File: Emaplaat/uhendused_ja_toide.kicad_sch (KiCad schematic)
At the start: 25 parts, among them IC4 FT232RNL-TUBE, IC5 TPS54429PWPR, J5 USB4216-03-A, J6 USB-A-S-VT, J7 USB-A-S-VT, J8 Barrel_Jack

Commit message: cleanoupp T__W
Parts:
- removed J7: USB-A-S-VT, USBASVT, symbol USB-A-S-VT:USB-A-S-VT
- added J1: USB-A-S-VT, USBASVT, symbol USB-A-S-VT:USB-A-S-VT
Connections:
- net 3V3: now also J1.1
- net AGND: now also J1.4, J1.MH, J1.MH1
- net RX_pult_2: now also J1.2
- net TX_pult_2: now also J1.3
- net at IC4.19 (RESET#): now also IC4.24 (NC_2), IC4.27 (OSCI), IC4.8 (NC_1)
- net TEST: now reaches IC4.26 (TEST)
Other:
- moved on the sheet: C21, C22, C23, C24, C25, C26, C27, C28, C29, C30, C31, C32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

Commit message: qqwertrewasdfgfdsdfgfdsdfgfdsasdfghgfdsdfghgfdsasdfghgfdsasdfgfew3
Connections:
- net TEST is gone; now on net AGND: IC4.26 (TEST)
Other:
- moved on the sheet: IC4

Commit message: enamvahem valmis
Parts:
- added C1: 100u, symbol Device:C
- added C2: 47u, symbol Device:C
- added D2, D3, D4, D5, D6, D7, D8: PESD1ETH10L-QYL, PESD1ETH10LQYL, symbol PESD1ETH10L-QYL:PESD1ETH10L-QYL
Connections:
- net 12V: now also C1.1, C2.1, D8.1 (K1)
- net 3V3: now also D2.1 (K1), D4.1 (K1)
- net AGND: now also D2.2 (K2), D3.2 (K2), D4.2 (K2), D5.2 (K2), D6.2 (K2), D7.2 (K2)
- net PGND: now also C1.2, C2.2, D8.2 (K2)
- net RX_pult_1: now also D3.1 (K1)
- net RX_pult_2: now also D5.1 (K1)
- net TX_pult_1: now also D6.1 (K1)
- net TX_pult_2: now also D7.1 (K1)
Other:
- note added: "Läpaka barrel connector"
- note added: "puldilt info lugemiseks usb A ühendused, koos ESD kaitsega"
- note removed: "puldilt info lugemiseks usb A ühendused"
- moved on the sheet: C21, C22, C23, C24, C25, C26, C27, C28, C29, C30, C31, C32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

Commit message: git stuff
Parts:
- removed D5, D6, D7, D8: PESD1ETH10L-QYL, PESD1ETH10LQYL, symbol PESD1ETH10L-QYL:PESD1ETH10L-QYL
- removed J1, J6: USB-A-S-VT, USBASVT, symbol USB-A-S-VT:USB-A-S-VT
- added C270: 0.1u, symbol Device:C
- added D15, D16: LED, LED_SMD:LED_0603_1608Metric, symbol Device:LED
- added D9: PESD1ETH10L-QYL, PESD1ETH10LQYL, symbol PESD1ETH10L-QYL:PESD1ETH10L-QYL
- added R208, R209: 5.1K, symbol Device:R
- added R210, R211: 50, Resistor_SMD:R_0603_1608Metric, symbol Device:R
- renumbered C27 to C20, C28 to C21, C29 to C22, C30 to C23, C31 to C24, C1 to C25, C2 to C26, C32 to C27, C33 to C28, C34 to C29, C35 to C30, C21 to C43, C22 to C44, C23 to C45, C24 to C46, C25 to C47, C26 to C48, IC4 to IC16, IC5 to IC9, J8 to J1, J5 to J2, L2 to L1, R6 to R23, R7 to R24, R8 to R25
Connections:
- net PGND is gone; now on net AGND: C20.2, C21.2, C22.2, C23.2, C24.2, C25.2, C26.2, C30.2, IC9.15 (PAD), IC9.8 (PGND1), IC9.9 (PGND2), J1.2
- net RX_pult_1 is gone; now on an unnamed net: D3.1 (K1)
- net 12V: now also D2.1 (K1)
- net 3V3: now also IC16.4 (VCCIO), C270.1, D15.2 (A), D16.2 (A); no longer D2.1 (K1), D4.1 (K1)
- net AGND: now also C270.2, D9.2 (K2), R208.2, R209.2; no longer IC16.26 (TEST), IC16.28 (OSCO), J2.A5 (CC1), J2.A8 (SBU1), J2.B5 (CC2), J2.B8 (SBU2)
- net at C43.1, C44.1, C45.1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: now also D9.1 (K1); no longer IC16.4 (VCCIO)
- net at C47.1, IC16.15 (USBDP), J2.A6 (DP1)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: now also D4.1 (K1)
- net at IC16.24 (NC_2), IC16.8 (NC_1): no longer IC16.19 (RESET#), IC16.27 (OSCI)
- new net: J2.B5 (CC2), R209.1
- new net: J2.A5 (CC1), R208.1
- new net: IC16.23 (CBUS0), R210.1
- new net: D15.1 (K), R210.2
- new net: IC16.22 (CBUS1), R211.1
- new net: J2.A8 (SBU1), J2.B8 (SBU2)
- new net: D16.1 (K), R211.2
- now unconnected: IC16.10 (DCD#), IC16.11 (CTS#), IC16.12 (CBUS4), IC16.13 (CBUS2), IC16.14 (CBUS3), IC16.2 (DTR#), IC16.3 (RTS#), IC16.6 (RI#), IC16.9 (DSR#)
- no-connect marks 0 -> 13
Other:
- note removed: "puldilt info lugemiseks usb A ühendused, koos ESD kaitsega"
- moved on the sheet: C20, C21, C22, C23, C24, C25, C26, C27, C28, C29, C30, C43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

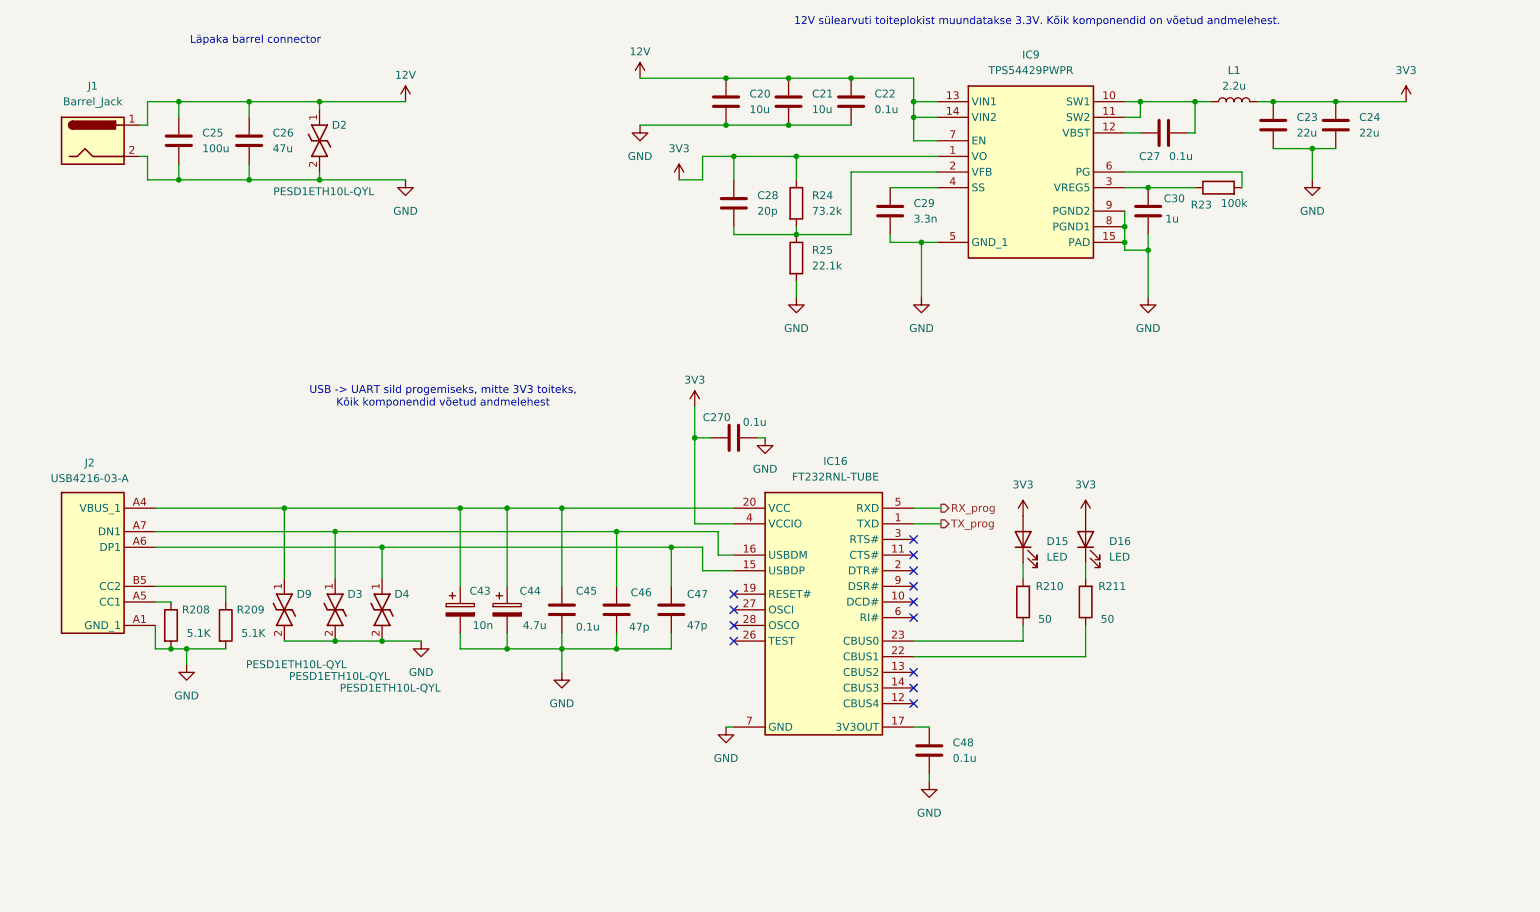
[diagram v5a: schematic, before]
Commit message: 3V3 voolud kontrollitud
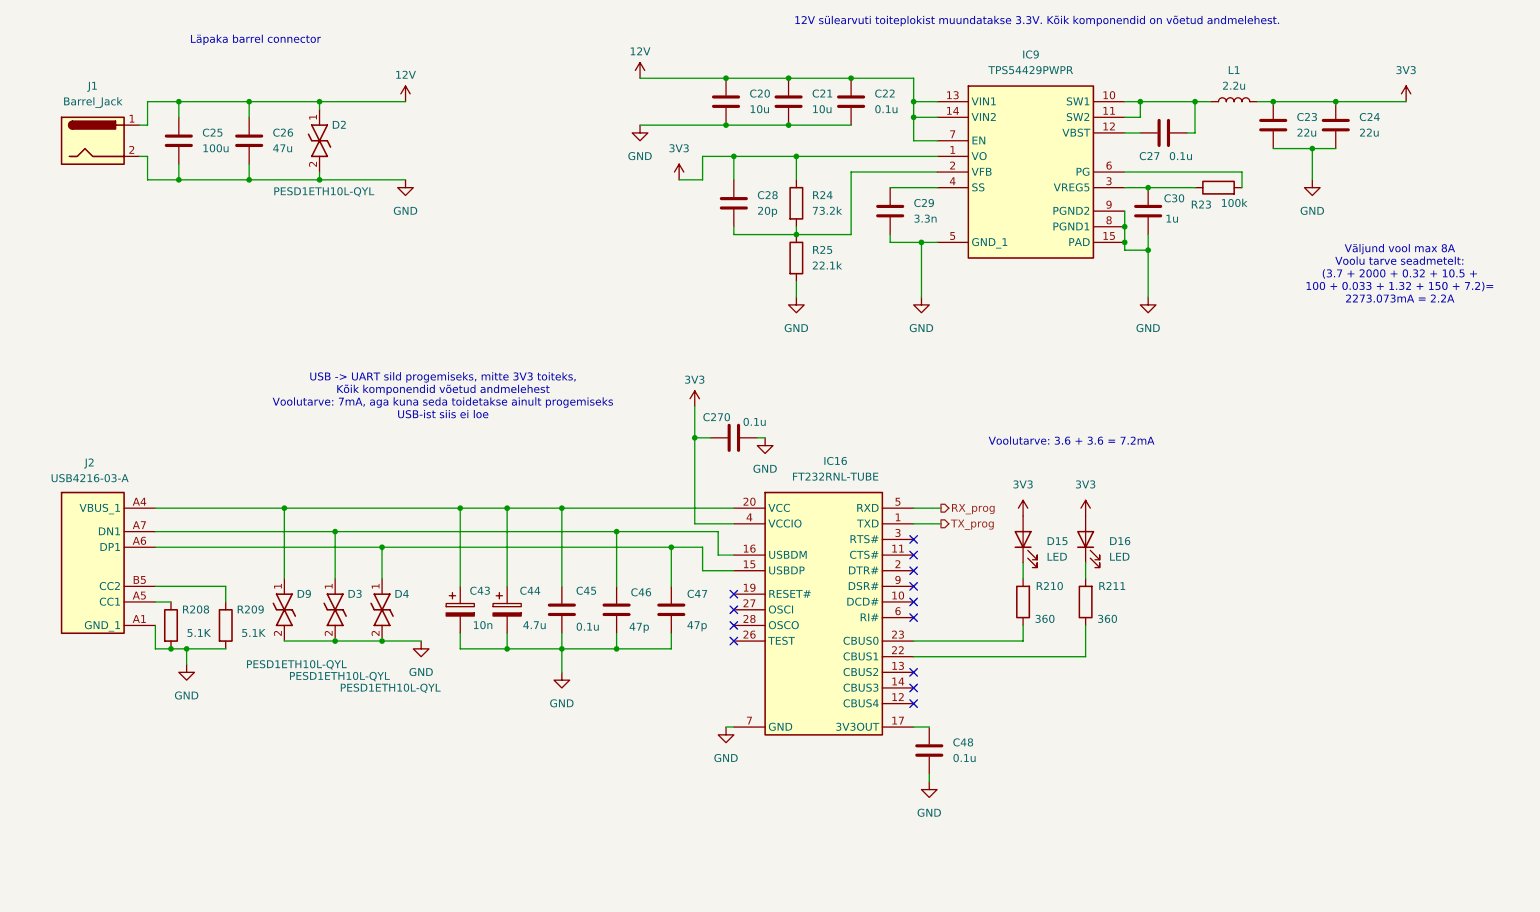
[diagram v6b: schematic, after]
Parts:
- R210, R211: value 50 -> 360
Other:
- note added: "USB -> UART sild progemiseks, mitte 3V3 toiteks, Kõik komponendid võetud andmelehest Voolutarve: 7mA, aga kuna seda toidetakse ainult progemiseks USB-ist siis ei loe"
- note added: "Voolutarve: 3.6 + 3.6 = 7.2mA"
- note added: "Väljund vool max 8A Voolu tarve seadmetelt: (3.7 + 2000 + 0.32 + 10.5 + 100 + 0.033 + 1.32 + 150 + 7.2)= 2273.073mA = 2.2A"
- note removed: "USB -> UART sild progemiseks, mitte 3V3 toiteks, Kõik komponendid võetud andmelehest"
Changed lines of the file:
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@@
 		)
 	)
-	(text "USB -> UART sild progemiseks, mitte 3V3 toiteks,\nKõik komponendid võetud andmelehest"
+	(text "Väljund vool max 8A\nVoolu tarve seadmetelt:\n(3.7 + 2000 + 0.32 + 10.5 + \n100 + 0.033 + 1.32 + 150 + 7.2)= \n2273.073mA = 2.2A"
+		(exclude_from_sim no)
+		(at 256.794 70.104 0)
+		(effects
+			(font
+				(size 1.27 1.27)
+			)
+		)
+	)
+	(text "USB -> UART sild progemiseks, mitte 3V3 toiteks,\nKõik komponendid võetud andmelehest\nVoolutarve: 7mA, aga kuna seda toidetakse ainult progemiseks \nUSB-ist siis ei loe"
 		(exclude_from_sim no)
 		(at 101.346 89.916 0)
@@
 		)
 	)
+	(text "Voolutarve: 3.6 + 3.6 = 7.2mA"
+		(exclude_from_sim no)
+		(at 203.454 97.282 0)
+		(effects
+			(font
+				(size 1.27 1.27)
+			)
+		)
+	)
 	(junction
 		(at 81.28 54.61)
@@
 			)
 		)
-		(property "Value" "50"
+		(property "Value" "360"
 			(at 199.136 125.984 0)
 			(effects
@@
 			)
 		)
-		(property "Value" "50"
+		(property "Value" "360"
 			(at 209.296 125.984 0)
 			(effects

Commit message: okei fix
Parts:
- removed D2, D3, D4, D9: PESD1ETH10L-QYL, PESD1ETH10LQYL, symbol PESD1ETH10L-QYL:PESD1ETH10L-QYL
- added D2, D3, D4, D9: CPDH3V3UP-HF, SODFL1608X77N, symbol CPDH3V3UP-HF:CPDH3V3UP-HF
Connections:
- net 12V: now also D2. (A)
- net AGND: now also D2. (A), D3. (A), D4. (A), D9. (A)
- net at C47.1, IC16.15 (USBDP), J2.A6 (DP1)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: now also D9. (A)
- net at C43.1, C44.1, C45.1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: now also D3. (A)
- net at C46.1, IC16.16 (USBDM), J2.A7 (DN1)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: now also D4. (A)
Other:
- note added: "C43 - HF Bypass C44 ja C45 - Decoupler C46 ja C47 - shunt ESDle"

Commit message: Kaareli kolmas tagasiside
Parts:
- removed C43: 10n, symbol Device:C_Polarized
- removed C44: 4.7u, symbol Device:C_Polarized
- removed C46, C47: 47p, symbol Device:C
- added C12: 4.7u, symbol Device:C
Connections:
- net 12V: no longer J1.1
- net AGND: now also C12.2
- net at C45.1, D3. (A), IC16.20 (VCC)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: now also C12.1
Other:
- note added: "Läpaka barrel connector barrel connectorile fuse receptacle"
- note removed: "Läpaka barrel connector"
- moved on the sheet: C25, C26, D2
